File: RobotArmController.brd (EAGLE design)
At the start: 63 parts, among them M1 M02LOCK, M2 M02LOCK, M3 M02LOCK, M4 M02LOCK, M5 M02LOCK, M6 M02LOCK

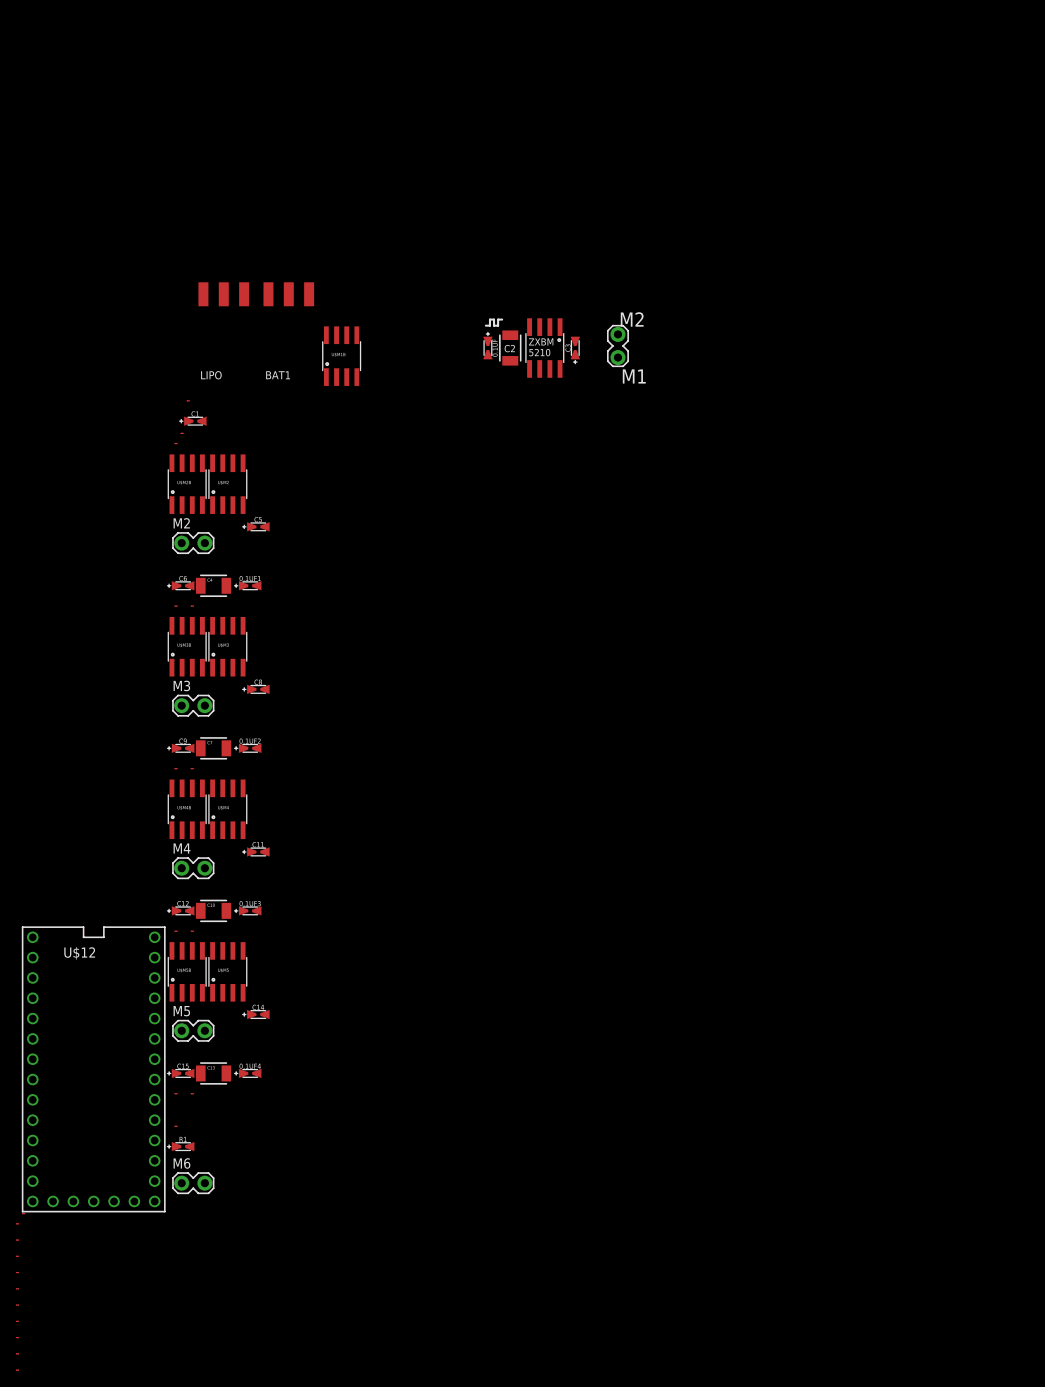
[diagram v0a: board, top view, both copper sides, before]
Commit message: Route motor drivers
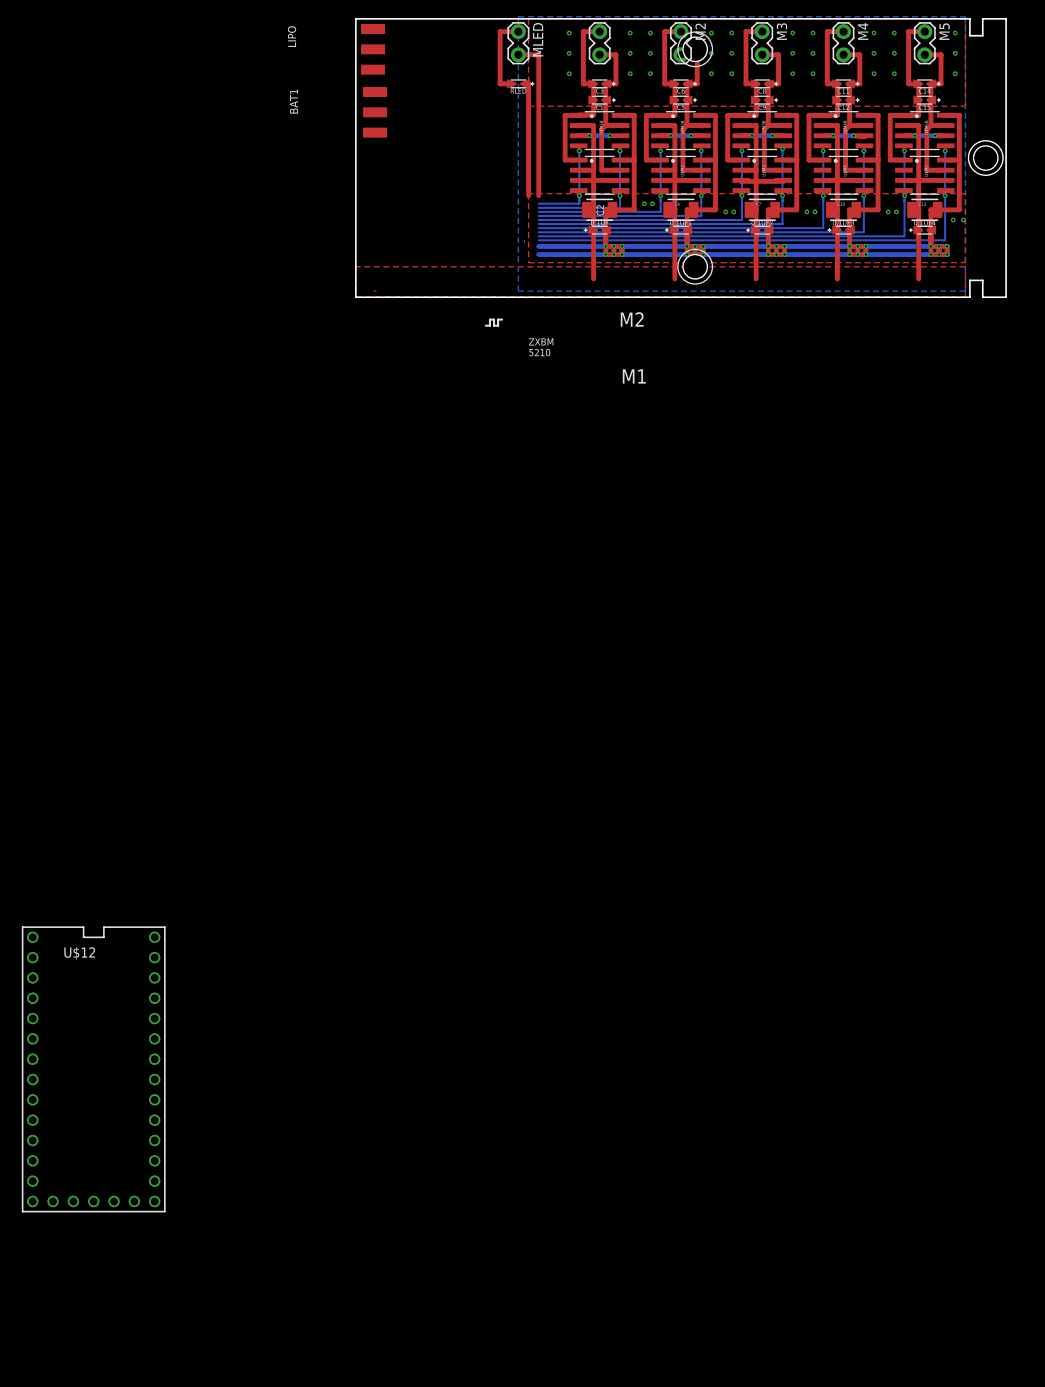
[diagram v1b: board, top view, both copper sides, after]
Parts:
- removed M6: M02LOCK, tekdemo:1X02_LOCK
- removed R1: (no value), tekdemo:0402-0603-0805-UNIVERSAL
- added MLED: M02LOCK, tekdemo:1X02_LOCK
- added RLED: (no value), tekdemo:0402-0603-0805-UNIVERSAL
- moved U$23 185.0 mm to (73.7, 22.1), flipped to the bottom, turned to 270 degrees
- moved U$22 180.4 mm to (68.6, 22.4), flipped to the bottom, turned to 270 degrees
- moved U$21 175.7 mm to (63.5, 22.4), flipped to the bottom, turned to 270 degrees
- moved U$20 171.1 mm to (58.4, 22.4), flipped to the bottom, turned to 270 degrees
- moved U$19 166.4 mm to (53.3, 22.4), flipped to the bottom, turned to 270 degrees
- moved U$18 161.9 mm to (48.3, 22.4), flipped to the bottom, turned to 270 degrees
- moved U$17 157.4 mm to (43.2, 22.4), flipped to the bottom, turned to 270 degrees
- moved M5 155.4 mm to (71.1, 43.2), turned to 270 degrees
- moved U$24 154.6 mm to (21.1, 17.0), turned to 90 degrees
- moved C15 153.0 mm to (71.1, 34.8), turned to 180 degrees
- moved U$16 153.0 mm to (38.1, 22.4), flipped to the bottom, turned to 270 degrees
- moved U$15 148.6 mm to (33.0, 22.4), flipped to the bottom, turned to 270 degrees
- moved U$14 144.6 mm to (27.9, 22.4), flipped to the bottom, turned to 270 degrees
- moved C14 143.1 mm to (71.1, 36.8), turned to 180 degrees
- moved U$10 141.9 mm to (70.4, 17.8), turned to 270 degrees
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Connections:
- removed net GND_M6: R1.+, U$13.P$2
- removed net M1: U$M1B.1
- removed net M10: U$M5B.7
- removed net M2: U$M1B.7
- removed net M3: U$M2B.1
- removed net M4: U$M2B.7
- removed net M5: U$M3B.1
- removed net M6: U$M3B.7
- removed net M7: U$M4B.1
- removed net M8: U$M4B.7
- removed net M9: U$M5B.1
- new net GND_LED: RLED.+, U$13.P$2
- new net N$10: U$22.P$1
- new net N$11: U$23.P$1
- new net N$2: U$15.P$1
- new net N$3: U$14.P$1
- new net N$4: U$16.P$1
- new net N$5: U$17.P$1
- new net N$6: U$19.P$1
- new net N$7: U$18.P$1
- new net N$8: U$21.P$1
- new net N$9: U$20.P$1
- net N$1: now also MLED.1, RLED.-; no longer M6.2, R1.-
- net T13/LED: now also MLED.2; no longer M6.1
- net VM1A: now also U$M1B.1
- net VM1B: now also U$M1B.7
- net VM2A: now also U$M2B.1
- net VM2B: now also U$M2B.7
- net VM3A: now also U$M3B.1
- net VM3B: now also U$M3B.7
- net VM4A: now also U$M4B.1
- net VM4B: now also U$M4B.7
- net VM5A: now also U$M5B.1
- net VM5B: now also U$M5B.7
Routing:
- net GND: track 0.00 -> 159.0 mm, vias 0 -> 70
- net N$11: track 0.00 -> 55.6 mm
- net N$10: track 0.00 -> 50.3 mm
- net N$8: track 0.00 -> 44.7 mm
- net N$9: track 0.00 -> 39.1 mm
- net N$6: track 0.00 -> 33.5 mm
- net VIN_M2: track 0.00 -> 30.7 mm, vias 0 -> 2
- net M2B: track 0.00 -> 29.9 mm, vias 0 -> 2
- net VIN_M3: track 0.00 -> 29.6 mm, vias 0 -> 2
- net VIN_M1: track 0.00 -> 29.4 mm, vias 0 -> 2
- net N$7: track 0.00 -> 27.9 mm
- net VIN_M5: track 0.00 -> 27.8 mm, vias 0 -> 2
- net VIN: track 0.00 -> 27.7 mm
- net VIN_M4: track 0.00 -> 27.6 mm, vias 0 -> 2
- net VM5A: track 0.00 -> 24.6 mm
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- added copper zone on layer 1, net GND
- added copper zone on layer 16, net GND
- added copper zone on layer 1, net VIN
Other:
- board outline added: 81.3 x 34.8 mm

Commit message: Route + Define mechanical
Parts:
- removed BAT1, LIPO: 1x3 RA Female .1", tekdemo:1X03_SMD_RA_FEMALE
- added JP1: M02JST-PTH-2, tekdemo:JST-2-PTH
- moved U$12 121.2 mm to (8.89, 27.4), turned to 180 degrees
- moved U$23 48.5 mm to (25.4, 17.3), turned to 0 degrees
- moved U$22 43.4 mm to (25.4, 17.8), turned to 0 degrees
- moved U$21 38.3 mm to (25.4, 18.3), turned to 0 degrees
- moved U$20 33.2 mm to (25.4, 18.8), turned to 0 degrees
- moved U$19 28.1 mm to (25.4, 19.3), turned to 0 degrees
- moved U$13 25.9 mm to (20.8, 43.7), flipped to the bottom, turned to 180 degrees
- moved U$18 23.0 mm to (25.4, 19.8), turned to 0 degrees
- moved U$17 17.9 mm to (25.4, 20.3), turned to 0 degrees
- moved U$16 12.8 mm to (25.4, 20.8), turned to 0 degrees
- moved U$4 11.4 mm to (13.7, 10.9)
- moved U$24 9.16 mm to (14.5, 10.7), turned to 180 degrees
- moved U$15 7.69 mm to (25.4, 21.3), turned to 0 degrees
- moved U$8 6.60 mm to (66.8, 18.0)
- moved 0.1UF4 6.60 mm to (77.7, 18.5)
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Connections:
- removed net N$10: U$22.P$1
- removed net N$11: U$23.P$1
- removed net N$2: U$15.P$1
- removed net N$3: U$14.P$1
- removed net N$4: U$16.P$1
- removed net N$5: U$17.P$1
- removed net N$6: U$19.P$1
- removed net N$7: U$18.P$1
- removed net N$8: U$21.P$1
- removed net N$9: U$20.P$1
- removed net T/6/PWM: U$12.6
- removed net VHALFBAT: BAT1.2
- new net T6/PWM: U$12.6, U$16.P$1
- net GND: now also JP1.1; no longer BAT1.1
- net GND_LED: now also MLED.1; no longer RLED.+
- net N$1: now also MLED.2; no longer MLED.1
- net T10/PWM: now also U$14.P$1
- net T13/LED: now also RLED.+; no longer MLED.2
- net T20/PWM: now also U$20.P$1
- net T21/PWM: now also U$21.P$1
- net T22/PWM: now also U$22.P$1
- net T23/PWM: now also U$23.P$1
- net T3/PWM: now also U$19.P$1
- net T4/PWM: now also U$18.P$1
- net T5/PWM: now also U$17.P$1
- net T9/PWM: now also U$15.P$1
- net VBAT: no longer BAT1.3, U$4.P$1
- net VIN: now also JP1.2, U$4.P$1
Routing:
- net M5B: track 8.03 -> 67.7 mm
- net N$11: track 55.6 -> 0.00 mm
- net M5A: track 7.77 -> 62.1 mm
- net N$10: track 50.3 -> 0.00 mm
- net M4B: track 7.77 -> 56.5 mm
- net N$8: track 44.7 -> 0.00 mm
- net M4A: track 7.77 -> 51.0 mm
- net N$9: track 39.1 -> 0.00 mm
- net N$6: track 33.5 -> 0.00 mm
- net M3B: track 7.77 -> 41.3 mm
- net M3A: track 7.77 -> 35.7 mm
- net N$7: track 27.9 -> 0.00 mm
- net T20/PWM: track 0.00 -> 27.2 mm
- net T21/PWM: track 0.00 -> 26.9 mm
- net T23/PWM: track 0.00 -> 26.8 mm
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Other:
- board size 81.3 x 34.8 mm -> 83.6 x 34.8 mm

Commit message: Wire to teensy
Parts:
- added JP2, JP3, JP4, JP5, JP6: (no value), tekdemo:1X03_LOCK
- moved RLED 2.41 mm to (20.3, 38.1), turned to 0 degrees
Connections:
- net 3.3V: now also JP2.2, JP3.2, JP4.2, JP5.2, JP6.2
- net GND: now also JP2.1, JP3.1, JP4.1, JP5.1, JP6.1
- net T15/A1: now also JP3.3
- net T16/A2: now also JP4.3
- net T17/A3: now also JP5.3
- net T18/A4: now also JP6.3
- net T19/A5: now also JP2.3
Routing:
- net 3.3V: track 0.00 -> 37.0 mm
- net T19/A5: track 7.72 -> 24.2 mm
- net T18/A4: track 8.24 -> 24.2 mm
- net T15/A1: track 8.26 -> 24.2 mm
- net T16/A2: track 8.26 -> 24.2 mm
- net T17/A3: track 8.71 -> 24.2 mm
- net T14/A0: track 8.26 -> 0.00 mm
- net N$1: track 3.89 -> 2.81 mm
- net T13/LED: track 22.0 -> 21.0 mm
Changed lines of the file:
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@@
 <element name="U$11" library="tekdemo" package="NET-JUNCTION-2" value="NET-JUNCTION-2" x="78.486" y="17.78" rot="R270"/>
 <element name="U$13" library="tekdemo" package="NET-JUNCTION-2" value="NET-JUNCTION-2" x="20.828" y="43.688" rot="MR180"/>
-<element name="RLED" library="tekdemo" package="0402-0603-0805-UNIVERSAL" value="" x="19.558" y="35.814" rot="R90"/>
+<element name="RLED" library="tekdemo" package="0402-0603-0805-UNIVERSAL" value="" x="20.32" y="38.1"/>
 <element name="MLED" library="tekdemo" package="1X02_LOCK" value="M02LOCK" x="19.558" y="43.18" rot="R270"/>
 <element name="U$12" library="Teensy_3_Series_Board_v1.0" package="TEENSY_3.1_BASIC" value="TEENSY_3.1_BASIC" x="8.89" y="27.432" rot="R180"/>
@@
 <attribute name="SKU" value="PRT-09914" x="74.676" y="13.462" size="1.778" layer="27" font="vector" ratio="15" rot="R270" display="off"/>
 </element>
+<element name="JP2" library="tekdemo" package="1X03_LOCK" value="" x="26.67" y="25.4" rot="R180"/>
+<element name="JP3" library="tekdemo" package="1X03_LOCK" value="" x="26.67" y="35.56" rot="R180"/>
+<element name="JP4" library="tekdemo" package="1X03_LOCK" value="" x="26.67" y="33.02" rot="R180"/>
+<element name="JP5" library="tekdemo" package="1X03_LOCK" value="" x="26.67" y="30.48" rot="R180"/>
+<element name="JP6" library="tekdemo" package="1X03_LOCK" value="" x="26.67" y="27.94" rot="R180"/>
 </elements>
 <signals>
@@
 <wire x1="21.844" y1="16.51" x2="19.558" y2="14.478" width="0.508" layer="16"/>
 <wire x1="19.558" y1="14.478" x2="19.558" y2="13.716" width="0.508" layer="16"/>
+<contactref element="JP6" pad="1"/>
+<contactref element="JP5" pad="1"/>
+<contactref element="JP4" pad="1"/>
+<contactref element="JP3" pad="1"/>
+<contactref element="JP2" pad="1"/>
 <wire x1="14.224" y1="10.668" x2="14.478" y2="10.668" width="0" layer="19" extent="1-1"/>
 <wire x1="15.494" y1="10.922" x2="14.478" y2="10.668" width="0" layer="19" extent="1-16"/>
@@
 </signal>
 <signal name="3.3V">
+<contactref element="JP6" pad="2"/>
+<contactref element="JP5" pad="2"/>
+<contactref element="JP4" pad="2"/>
+<contactref element="JP3" pad="2"/>
+<contactref element="JP2" pad="2"/>
+<wire x1="5.08" y1="19.812" x2="18.669" y2="19.812" width="0.508" layer="1"/>
+<wire x1="18.669" y1="19.812" x2="24.13" y2="25.527" width="0.508" layer="1"/>
+<wire x1="24.13" y1="25.527" x2="24.13" y2="28.067" width="0.508" layer="1"/>
+<wire x1="24.13" y1="28.067" x2="24.13" y2="30.607" width="0.508" layer="1"/>
+<wire x1="24.13" y1="30.607" x2="24.13" y2="33.147" width="0.508" layer="1"/>
+<wire x1="24.13" y1="33.147" x2="24.13" y2="35.687" width="0.508" layer="1"/>
+<contactref element="U$12" pad="3.3V"/>
 <contactref element="U$12" pad="3.3V1"/>
-<contactref element="U$12" pad="3.3V"/>
-<wire x1="1.27" y1="16.002" x2="11.43" y2="43.942" width="0" layer="19" extent="1-1"/>
+<wire x1="1.27" y1="16.002" x2="5.08" y2="19.812" width="0.508" layer="1"/>
+<wire x1="24.13" y1="35.687" x2="11.43" y2="43.942" width="0" layer="19" extent="1-1"/>
 </signal>
 <signal name="T3/PWM" class="1">
@@
 <wire x1="15.24" y1="16.764" x2="15.494" y2="17.018" width="0.254" layer="16"/>
 <wire x1="15.494" y1="17.018" x2="17.78" y2="17.018" width="0.1524" layer="16"/>
-<wire x1="17.78" y1="17.018" x2="18.796" y2="17.78" width="0.254" layer="16"/>
-<wire x1="18.796" y1="17.78" x2="25.4" y2="17.78" width="0.254" layer="16"/>
+<wire x1="17.78" y1="17.018" x2="18.542" y2="17.78" width="0.254" layer="16"/>
+<wire x1="18.542" y1="17.78" x2="25.4" y2="17.78" width="0.254" layer="16"/>
 <contactref element="U$22" pad="P$1"/>
 </signal>
@@
 <signal name="T19/A5" class="1">
 <contactref element="U$12" pad="19/A5"/>
-<wire x1="1.27" y1="28.702" x2="4.572" y2="25.4" width="0.254" layer="1"/>
-<wire x1="4.572" y1="25.4" x2="7.62" y2="25.4" width="0.254" layer="1"/>
+<wire x1="1.27" y1="28.702" x2="7.62" y2="22.352" width="0.254" layer="1"/>
+<wire x1="7.62" y1="22.352" x2="18.669" y2="22.352" width="0.254" layer="1"/>
+<contactref element="JP2" pad="3"/>
+<wire x1="18.669" y1="22.352" x2="21.59" y2="25.273" width="0.254" layer="1"/>
 </signal>
 <signal name="T18/A4" class="1">
 <contactref element="U$12" pad="18/A4"/>
-<wire x1="1.27" y1="31.242" x2="5.842" y2="26.67" width="0.254" layer="1"/>
-<wire x1="5.842" y1="26.67" x2="7.62" y2="26.67" width="0.254" layer="1"/>
+<wire x1="1.27" y1="31.242" x2="7.62" y2="24.892" width="0.254" layer="1"/>
+<wire x1="7.62" y1="24.892" x2="18.669" y2="24.892" width="0.254" layer="1"/>
+<contactref element="JP6" pad="3"/>
+<wire x1="18.669" y1="24.892" x2="21.59" y2="27.813" width="0.254" layer="1"/>
 </signal>
 <signal name="T4/PWM" class="1">
@@
 <wire x1="15.24" y1="17.78" x2="15.494" y2="17.526" width="0.254" layer="16"/>
 <wire x1="15.494" y1="17.526" x2="17.526" y2="17.526" width="0.1524" layer="16"/>
-<wire x1="17.526" y1="17.526" x2="18.542" y2="18.288" width="0.254" layer="16"/>
-<wire x1="18.542" y1="18.288" x2="25.4" y2="18.288" width="0.254" layer="16"/>
+<wire x1="17.526" y1="17.526" x2="18.288" y2="18.288" width="0.254" layer="16"/>
+<wire x1="18.288" y1="18.288" x2="25.4" y2="18.288" width="0.254" layer="16"/>
 <contactref element="U$21" pad="P$1"/>
 </signal>
 <signal name="T17/A3" class="1">
 <contactref element="U$12" pad="17/A3"/>
-<wire x1="1.27" y1="33.782" x2="6.35" y2="28.702" width="0.254" layer="1"/>
-<wire x1="6.35" y1="28.702" x2="7.874" y2="28.702" width="0.254" layer="1"/>
+<wire x1="1.27" y1="33.782" x2="7.62" y2="27.432" width="0.254" layer="1"/>
+<wire x1="7.62" y1="27.432" x2="18.669" y2="27.432" width="0.254" layer="1"/>
+<contactref element="JP5" pad="3"/>
+<wire x1="18.669" y1="27.432" x2="21.59" y2="30.353" width="0.254" layer="1"/>
 </signal>
 <signal name="T16/A2" class="1">
 <contactref element="U$12" pad="16/A2"/>
-<wire x1="1.27" y1="36.322" x2="7.112" y2="30.48" width="0.254" layer="1"/>
+<wire x1="1.27" y1="36.322" x2="7.62" y2="29.972" width="0.254" layer="1"/>
+<wire x1="7.62" y1="29.972" x2="18.669" y2="29.972" width="0.254" layer="1"/>
+<contactref element="JP4" pad="3"/>
+<wire x1="18.669" y1="29.972" x2="21.59" y2="32.893" width="0.254" layer="1"/>
 </signal>
 <signal name="T15/A1" class="1">
 <contactref element="U$12" pad="15/A1"/>
-<wire x1="1.27" y1="38.862" x2="7.112" y2="33.02" width="0.254" layer="1"/>
+<wire x1="1.27" y1="38.862" x2="7.62" y2="32.512" width="0.254" layer="1"/>
+<wire x1="7.62" y1="32.512" x2="18.669" y2="32.512" width="0.254" layer="1"/>
+<contactref element="JP3" pad="3"/>
+<wire x1="18.669" y1="32.512" x2="21.59" y2="35.433" width="0.254" layer="1"/>
 </signal>
 <signal name="T14/A0" class="1">
 <contactref element="U$12" pad="14/A0"/>
-<wire x1="1.27" y1="41.402" x2="7.112" y2="35.56" width="0.254" layer="1"/>
 </signal>
 <signal name="T13/LED" class="1">
 <contactref element="U$12" pad="13"/>
 <contactref element="RLED" pad="+"/>
-<wire x1="1.27" y1="43.942" x2="10.16" y2="35.052" width="0.254" layer="1"/>
-<wire x1="10.16" y1="35.052" x2="19.558" y2="35.052" width="0.254" layer="1"/>
+<wire x1="1.27" y1="43.942" x2="7.62" y2="37.592" width="0.254" layer="1"/>
+<wire x1="7.62" y1="37.592" x2="18.034" y2="37.592" width="0.254" layer="1"/>
+<wire x1="18.034" y1="37.592" x2="19.558" y2="38.1" width="0.254" layer="1"/>
 </signal>
 <signal name="T6/PWM" class="1">
@@
 <contactref element="MLED" pad="2"/>
 <contactref element="RLED" pad="-"/>
-<wire x1="19.558" y1="36.576" x2="19.558" y2="40.4622" width="0.254" layer="1"/>
+<wire x1="21.082" y1="38.1" x2="19.558" y2="40.4622" width="0.254" layer="1"/>
 </signal>
 <signal name="GND_LED" class="1">
